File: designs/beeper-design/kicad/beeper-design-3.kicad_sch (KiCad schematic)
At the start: 37 parts, among them J1 TC2030-IDC-NL, J6 10103594-0001LF, U1 DA14705-00000HZ2, U2 AT25FF321A-UUN-T, U7 TPD4S012DRYR

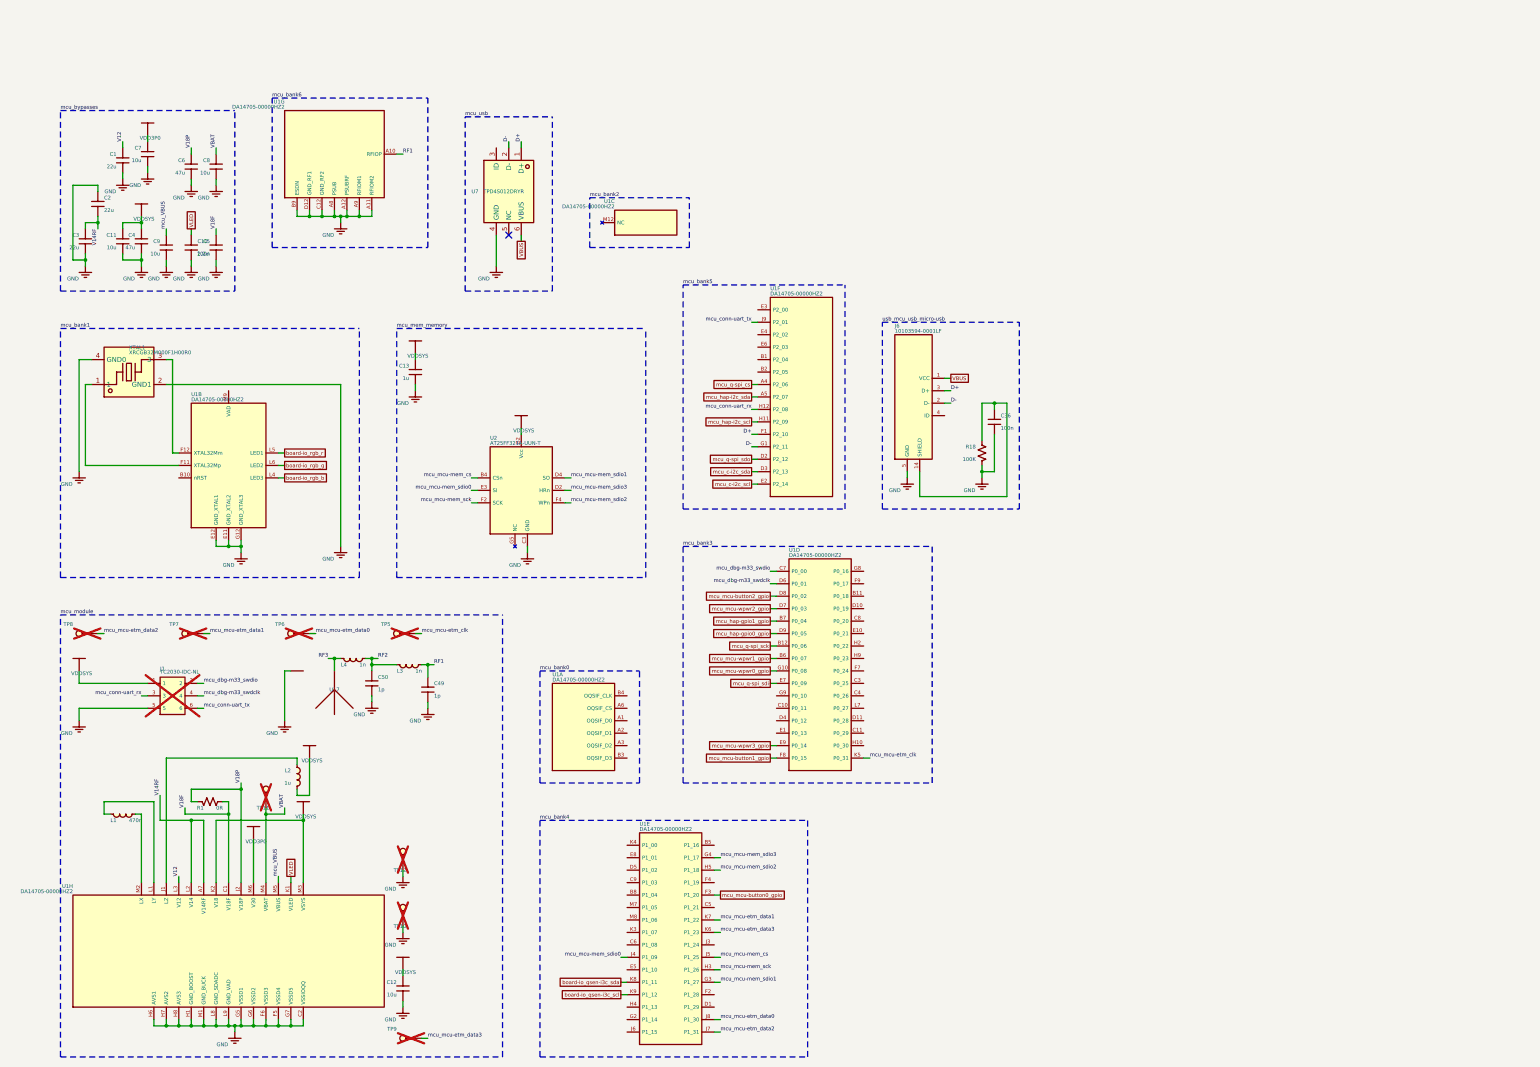
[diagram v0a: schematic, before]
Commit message: better export + JLCPCB numbers
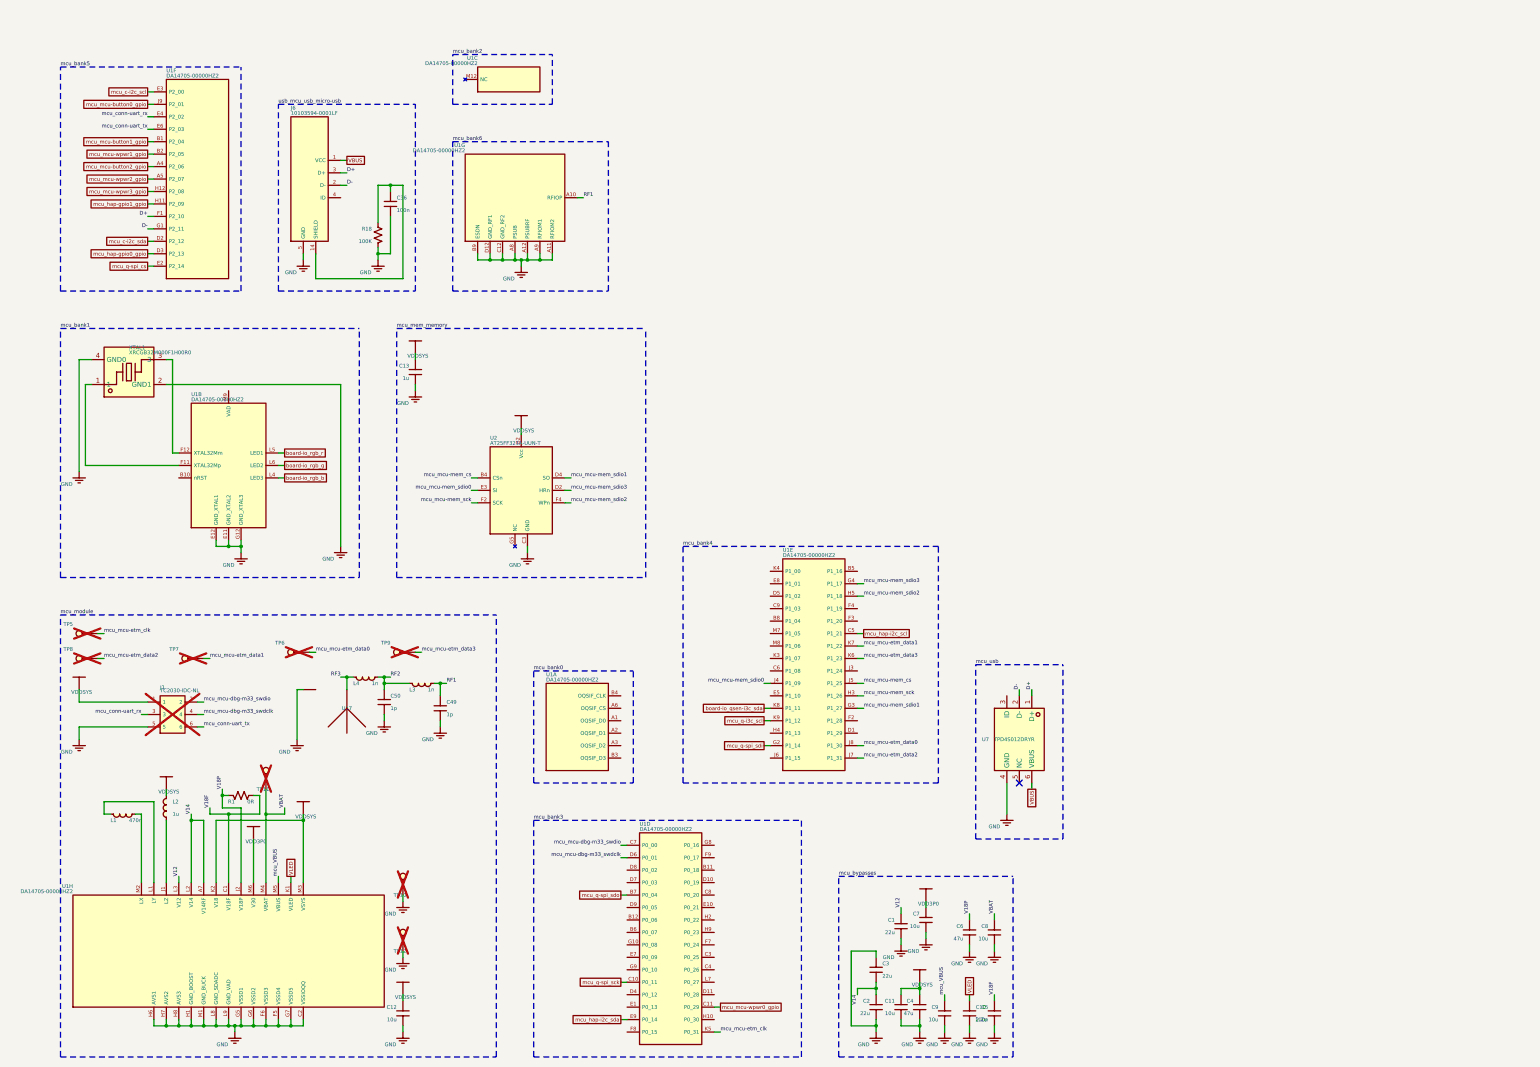
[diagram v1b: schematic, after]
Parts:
- removed C1: 22u, beeper-design:Pkg0603, symbol C86295
- removed C10: 2.2u, beeper-design:Pkg0201_18, symbol C318539_1
- removed C11: 10u, beeper-design:Pkg0402_6, symbol C962143_2
- removed C12: 10u, beeper-design:Pkg0402_5, symbol C962143_1
- removed C13: 1u, beeper-design:Pkg0201_34, symbol C76935_10
- removed C2: 22u, beeper-design:Pkg0603_1, symbol C86295_1
- removed C3: 22u, beeper-design:Pkg0603_2, symbol C86295_2
- removed C36: 100n, beeper-design:Pkg0201_31, symbol my_capacitor_6
- removed C4: 47u, beeper-design:Pkg0805_1, symbol my_capacitor_8
- removed C49: 1p, beeper-design:Pkg0201_39, symbol C277491_1
- removed C5: 100n, beeper-design:Pkg0201_7, symbol my_capacitor_1
- removed C50: 1p, beeper-design:Pkg0201_9, symbol C277491
- removed C6: 47u, beeper-design:Pkg0805, symbol my_capacitor_4
- removed C7: 10u, beeper-design:Pkg0402_7, symbol C962143_3
- removed C8: 10u, beeper-design:Pkg0402_9, symbol C962143_5
- removed C9: 10u, beeper-design:Pkg0402_3, symbol C962143
- added C1: 22u, beeper-design:Pkg0603, symbol C86295_2
- added C10: 2.2u, beeper-design:Pkg0201_11, symbol C318539
- added C11: 10u, beeper-design:Pkg0402_1, symbol C962143_1
- added C12: 10u, beeper-design:Pkg0402, symbol C962143
- added C13: 1u, beeper-design:Pkg0201_27, symbol C76935_7
- added C2: 22u, beeper-design:Pkg0603_1, symbol C86295
- added C3: 22u, beeper-design:Pkg0603_2, symbol C86295_1
- added C36: 100n, beeper-design:Pkg0201_24, symbol my_capacitor_3
- added C4: 47u, beeper-design:Pkg0805_1, symbol my_capacitor_5
- added C49: 1p, beeper-design:Pkg0201_32, symbol C277491
- added C5: 100n, beeper-design:Pkg0201, symbol my_capacitor_8
- added C50: 1p, beeper-design:Pkg0201_2, symbol C277491_1
- added C6: 47u, beeper-design:Pkg0805, symbol my_capacitor_1
- added C7: 10u, beeper-design:Pkg0402_2, symbol C962143_2
- added C8: 10u, beeper-design:Pkg0402_4, symbol C962143_4
- added C9: 10u, beeper-design:Pkg0402_9, symbol C962143_5
- L2: footprint beeper-design:Pkg0402_1 -> beeper-design:Pkg0402_7
- L3: footprint beeper-design:Pkg0201_1 -> beeper-design:Pkg0201_40
- L4: footprint beeper-design:Pkg0201_16 -> beeper-design:Pkg0201_9
- R1: footprint beeper-design:Pkg0201_25 -> beeper-design:Pkg0201_18
- R18: footprint beeper-design:Pkg0201_20 -> beeper-design:Pkg0201_13
- U1: footprint beeper-design:LP_1 -> beeper-design:LP
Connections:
- net GND: now also C1.1, C10.1, C11.1, C12.1, C13.1, C2.1, C3.1, C36.2, C4.1, C49.2, C5.1, C50.2, C6.1, C7.1, C8.1, C9.1
- net RF1: now also C49.1
- net RF2: now also C50.1
- net V12: now also C1.2
- net V18F: now also C5.2
- net V18P: now also C6.2
- net VBAT: now also C8.2
- net VDD3P0: now also C7.2
- net VDDSYS: now also C11.2, C12.2, C13.2, C4.2
- net VLED: now also C10.2
- net mcu_VBUS: now also C9.2
- net mcu_c-i2c_scl: now also U1.E3 (P2_00); no longer U1.E2 (P2_14)
- net mcu_c-i2c_sda: now also U1.D2 (P2_12); no longer U1.D3 (P2_13)
- net mcu_conn-uart_rx: now also U1.E4 (P2_02); no longer U1.H12 (P2_08)
- net mcu_conn-uart_tx: now also U1.E6 (P2_03); no longer U1.J9 (P2_01)
- net mcu_hap-gpio0_gpio: now also U1.D3 (P2_13); no longer U1.D9 (P0_05)
- net mcu_hap-gpio1_gpio: now also U1.H11 (P2_09); no longer U1.B7 (P0_04)
- net mcu_hap-i2c_scl: now also U1.C5 (P1_21); no longer U1.H11 (P2_09)
- net mcu_hap-i2c_sda: now also U1.E9 (P0_14); no longer U1.A5 (P2_07)
- net mcu_mcu-button0_gpio: now also U1.J9 (P2_01); no longer U1.F3 (P1_20)
- net mcu_mcu-button1_gpio: now also U1.B1 (P2_04); no longer U1.F8 (P0_15)
- net mcu_mcu-button2_gpio: now also U1.A4 (P2_06); no longer U1.D8 (P0_02)
- net mcu_mcu-wpwr0_gpio: now also U1.C11 (P0_29); no longer U1.G10 (P0_08)
- net mcu_mcu-wpwr1_gpio: now also U1.B2 (P2_05); no longer U1.B6 (P0_07)
- net mcu_mcu-wpwr2_gpio: now also U1.A5 (P2_07); no longer U1.D7 (P0_03)
- net mcu_mcu-wpwr3_gpio: now also U1.H12 (P2_08); no longer U1.E9 (P0_14)
- net mcu_q-spi_cs: now also U1.E2 (P2_14); no longer U1.A4 (P2_06)
- net mcu_q-spi_sck: now also U1.C10 (P0_11); no longer U1.B12 (P0_06)
- net mcu_q-spi_sdi: now also U1.G2 (P1_14); no longer U1.E7 (P0_09)
- net mcu_q-spi_sdo: now also U1.B7 (P0_04); no longer U1.D2 (P2_12)
- net at J6.10 (SHIELD), J6.11 (SHIELD), J6.13 (SHIELD)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: now also C36.1
- net V14RF renamed V14
- net V14: now also C2.2, C3.2
- net board-io_qsen-i3c_scl renamed mcu_q-i3c_scl
- net mcu_dbg-m33_swdclk renamed mcu_mcu-dbg-m33_swdclk
- net mcu_dbg-m33_swdio renamed mcu_mcu-dbg-m33_swdio

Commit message: post export, had to munge sch
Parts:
- removed C1: 22u, beeper-design:Pkg0603, symbol C86295_2
- removed C10: 2.2u, beeper-design:Pkg0201_11, symbol C318539
- removed C11: 10u, beeper-design:Pkg0402_1, symbol C962143_1
- removed C12: 10u, beeper-design:Pkg0402, symbol C962143
- removed C13: 1u, beeper-design:Pkg0201_27, symbol C76935_7
- removed C2: 22u, beeper-design:Pkg0603_1, symbol C86295
- removed C3: 22u, beeper-design:Pkg0603_2, symbol C86295_1
- removed C36: 100n, beeper-design:Pkg0201_24, symbol my_capacitor_3
- removed C4: 47u, beeper-design:Pkg0805_1, symbol my_capacitor_5
- removed C49: 1p, beeper-design:Pkg0201_32, symbol C277491
- removed C5: 100n, beeper-design:Pkg0201, symbol my_capacitor_8
- removed C50: 1p, beeper-design:Pkg0201_2, symbol C277491_1
- removed C6: 47u, beeper-design:Pkg0805, symbol my_capacitor_1
- removed C7: 10u, beeper-design:Pkg0402_2, symbol C962143_2
- removed C8: 10u, beeper-design:Pkg0402_4, symbol C962143_4
- removed C9: 10u, beeper-design:Pkg0402_9, symbol C962143_5
- removed J1: TC2030-IDC-NL, beeper-design:TC2030_IDC_NL_FOOTPRINT, symbol component
- removed J6: 10103594-0001LF, beeper-design:AMPHENOL_10103594_0001LF, symbol AMPHENOL_10103594_0001LF
- removed L1: 470n, beeper-design:Pkg0603_3, symbol C275359
- removed L2: 1u, beeper-design:Pkg0402_7, symbol C516791
- removed L3: 1n, beeper-design:Pkg0201_40, symbol C2041448_1
- removed L4: 1n, beeper-design:Pkg0201_9, symbol C2041448
- removed R1: 0R, beeper-design:Pkg0201_18, symbol C106228
- removed R18: 100K, beeper-design:Pkg0201_13, symbol C106230
- removed TP10, TP11, TP12, TP5, TP6, TP7, TP8, TP9: (no value), beeper-design:SMD_TESTPT, symbol smd_testpoint_cmp
- removed U1: DA14705-00000HZ2, beeper-design:LP, symbol DA14705
- removed U17: (no value), beeper-design:Pkg_2450AT18D0100_STD_R_1, symbol Sym2450AT18D0100
- removed U2: AT25FF321A-UUN-T, beeper-design:WLCSP_12, symbol AT25FF321A_UUN_T
- removed U7: TPD4S012DRYR, beeper-design:SON_6_L1_5_W1_0_P0_50_BL, symbol C96506
- removed XTAL1: XRCGB32M000F1H00R0, beeper-design:CRYSTAL_SMD_4P_L2_0_W1_6_BL_1, symbol C880116
- added C47: 1u, beeper-design:Pkg0201_40, symbol C76935_11
- added C48: 1u, beeper-design:Pkg0201_6, symbol C76935_2
- added R16, R17: 8K2, beeper-design:Pkg0201_20, symbol my_resistor_6
- added TP1, TP2: (no value), beeper-design:SMD_TESTPT, symbol smd_testpoint_cmp
- added U12: DRV2605YZFR, beeper-design:LP_8, symbol DRV2605YZFR
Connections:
- net GND: now also C47.1, C48.1, U12.B3 (GND)
- net mcu_hap-gpio0_gpio: now also U12.A1 (EN)
- net mcu_hap-gpio1_gpio: now also U12.B1 (IN_TRIG)
- net mcu_hap-i2c_scl: now also R17.1, U12.C1 (SCL)
- net mcu_hap-i2c_sda: now also R16.1, U12.B2 (SDA)
- new net: TP1.p, U12.A3 (OUT+)
- new net: C47.2, U12.A2 (REG)
- new net: TP2.p, U12.C3 (OUT-)
- new net VDD1P8: C48.2, R16.2, R17.2, U12.C2 (VDD)
- no-connect marks 1 -> 0
